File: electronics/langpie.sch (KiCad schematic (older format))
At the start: 0 parts

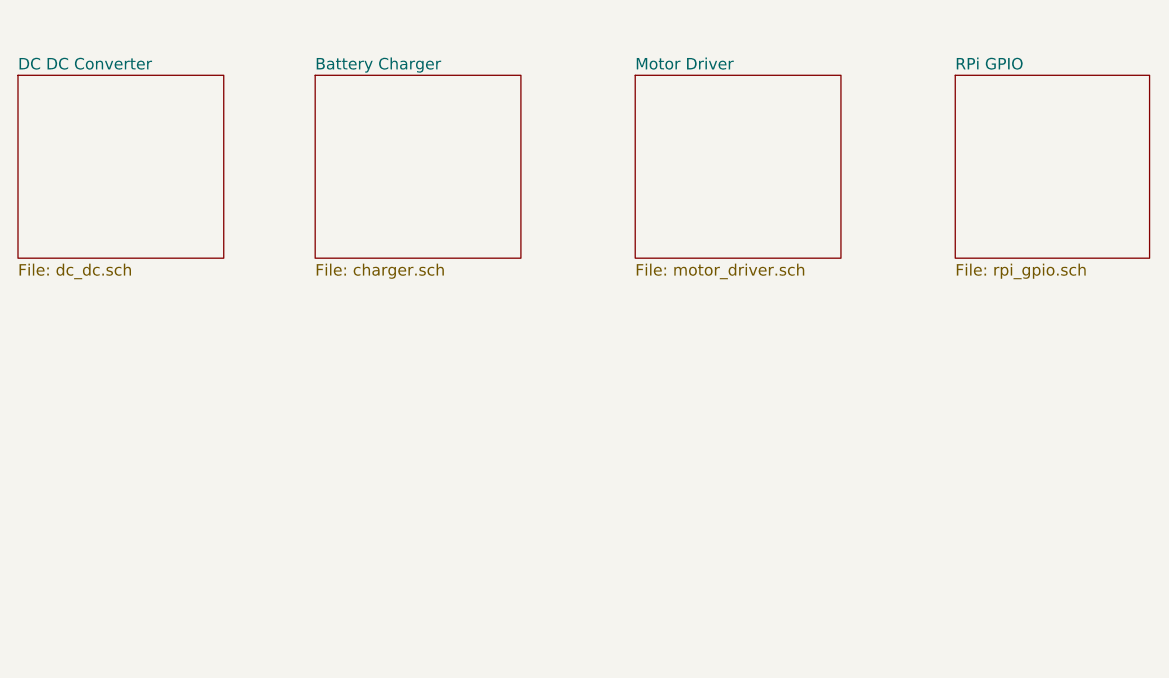
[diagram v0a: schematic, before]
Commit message: Change to electronics, and adding pi dimensions into documents
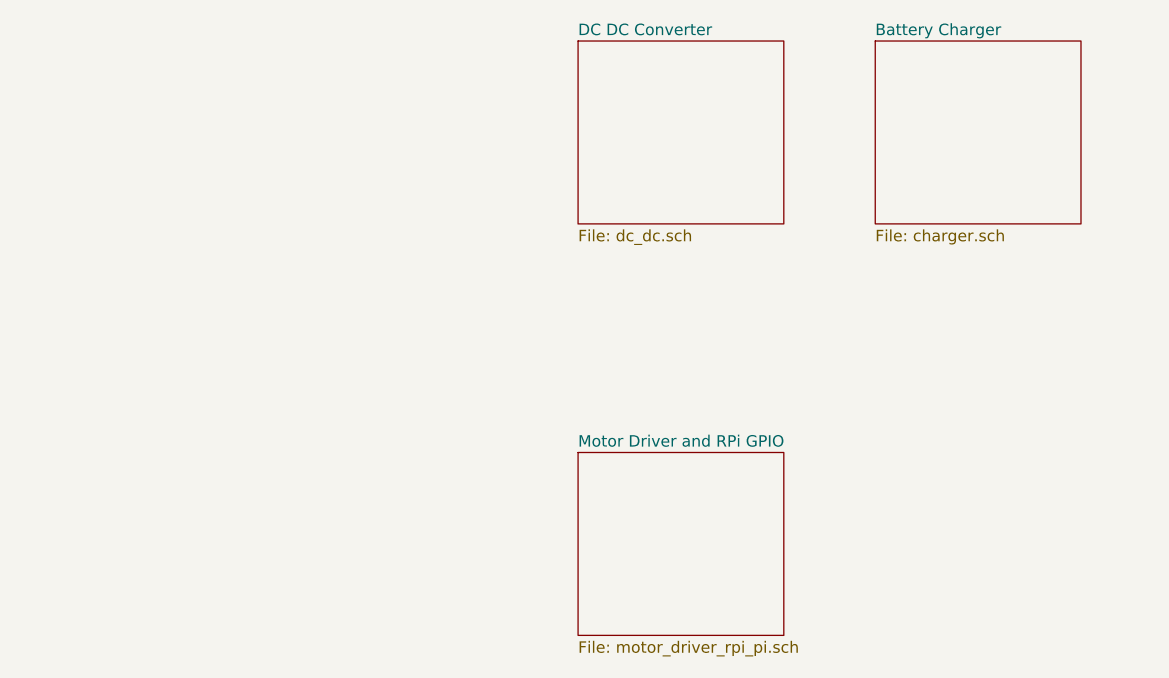
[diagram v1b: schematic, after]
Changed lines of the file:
@@
 $Descr A4 11693 8268
 encoding utf-8
-Sheet 1 5
+Sheet 1 4
 Title ""
 Date ""
@@
 $EndDescr
 $Sheet
-S 2350 2200 900  800
+S 4800 2050 900  800
 U 5E90B2B2
 F0 "DC DC Converter" 50
@@
 $EndSheet
 $Sheet
-S 3650 2200 900  800
+S 6100 2050 900  800
 U 5E915994
 F0 "Battery Charger" 50
@@
 $EndSheet
 $Sheet
-S 5050 2200 900  800
+S 4800 3850 900  800
 U 5E914BA5
-F0 "Motor Driver" 50
-F1 "motor_driver.sch" 50
-$EndSheet
-$Sheet
-S 6450 2200 850  800
-U 5E9108BA
-F0 "RPi GPIO" 50
-F1 "rpi_gpio.sch" 50
+F0 "Motor Driver and RPi GPIO" 50
+F1 "motor_driver_rpi_pi.sch" 50
 $EndSheet
 $EndSCHEMATC

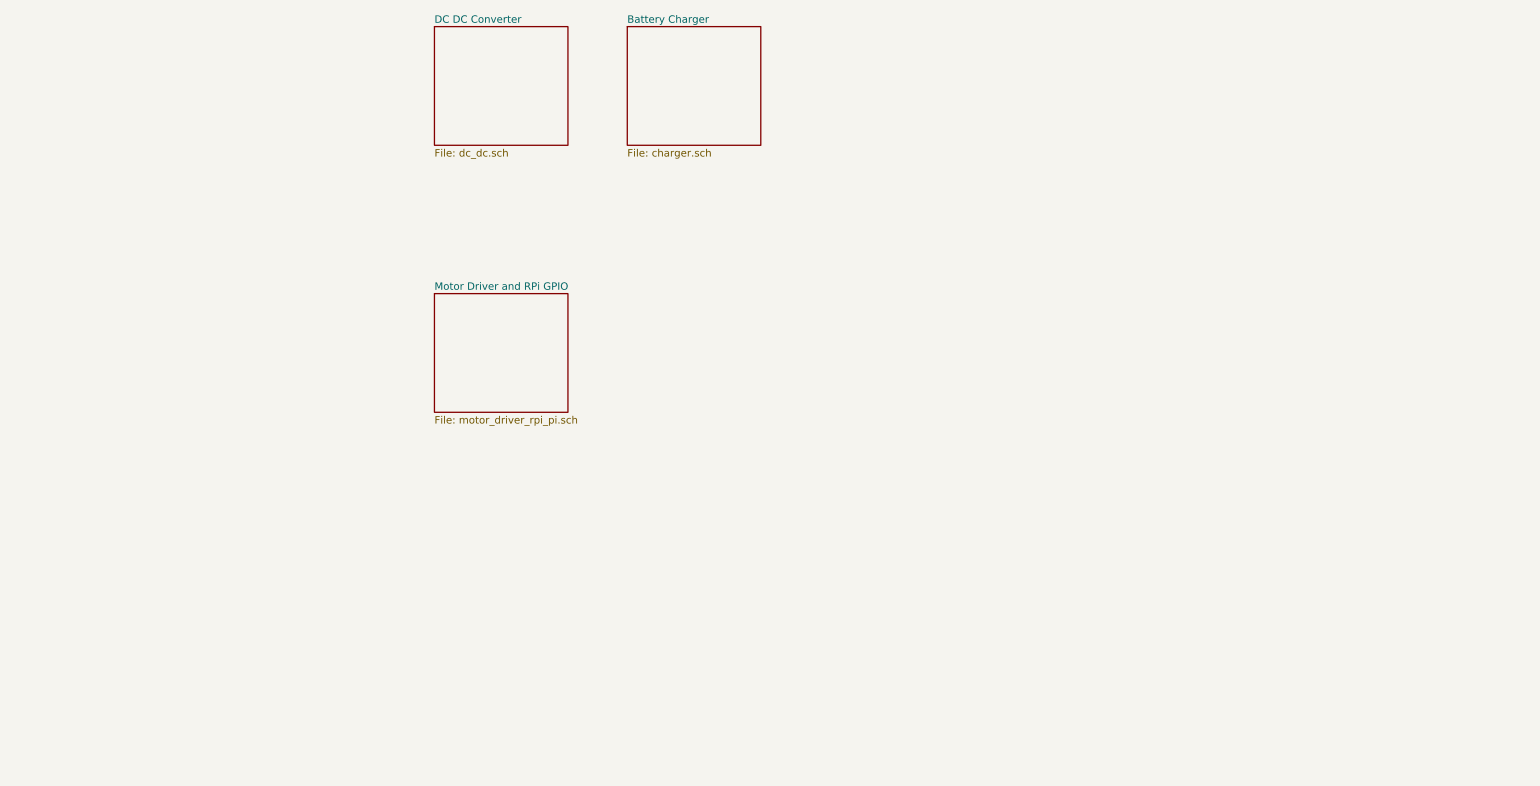
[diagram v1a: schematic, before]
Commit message: Preview SCH is done, but not fully finished.
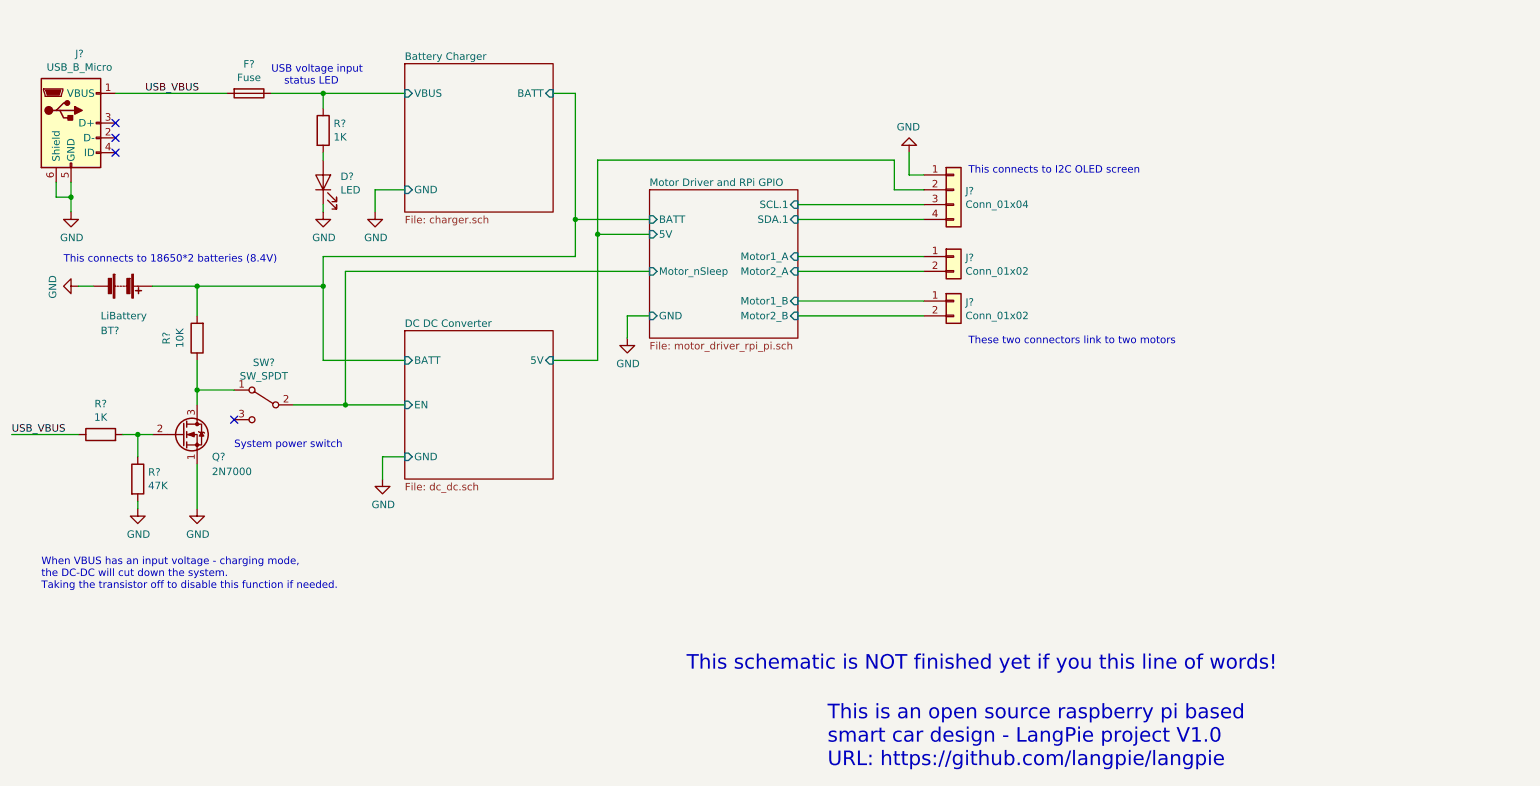
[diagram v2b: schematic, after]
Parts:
- added BT?: LiBattery, symbol Device:Battery
- added D?: LED, LED_SMD:LED_0805_2012Metric, symbol Device:LED
- added F?: Fuse, Fuse:Fuse_1206_3216Metric, symbol Device:Fuse
- added J?: USB_B_Micro, Connector_USB:USB_Micro-B_GCT_USB3076-30-A, symbol Connector:USB_B_Micro
- added J? (x2): Conn_01x02, Connector_Wire:SolderWirePad_1x02_P5.08mm_Drill1.5mm, symbol Connector_Generic:Conn_01x02
- added J?: Conn_01x04, Connector_PinHeader_2.54mm:PinHeader_1x04_P2.54mm_Vertical, symbol Connector_Generic:Conn_01x04
- added Q?: 2N7000, Package_TO_SOT_SMD:SOT-23, symbol Transistor_FET:2N7000
- added R? (x2): 1K, Resistor_SMD:R_0805_2012Metric, symbol Device:R
- added R?: 47K, Resistor_SMD:R_0805_2012Metric, symbol Device:R
- added R?: 10K, Resistor_SMD:R_0805_2012Metric, symbol Device:R
- added SW?: SW_SPDT, symbol Switch:SW_SPDT
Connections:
- new net: Q?.2 (G), R?.1, R?.2
- new net: Q?.3 (D), R?.1, SW?.1 (A)
- new net: D?.2 (A), R?.2
- new net Battery Charger/BATT: BT?.1 (+), R?.2
- new net Battery Charger/VBUS: F?.1, R?.1
- new net DC DC Converter/5V: J?.2 (Pin_2)
- new net DC DC Converter/EN: SW?.2 (B)
- new net GND: BT?.2 (-), D?.1 (K), J?.1 (Pin_1), J?.5 (GND), J?.6 (Shield), Q?.1 (S), R?.2
- new net Motor Driver and RPi GPIO/Motor1_A: J?.1 (Pin_1)
- new net Motor Driver and RPi GPIO/Motor1_B: J?.1 (Pin_1)
- new net Motor Driver and RPi GPIO/Motor2_A: J?.2 (Pin_2)
- new net Motor Driver and RPi GPIO/Motor2_B: J?.2 (Pin_2)
- new net Motor Driver and RPi GPIO/SCL.1: J?.3 (Pin_3)
- new net Motor Driver and RPi GPIO/SDA.1: J?.4 (Pin_4)
- new net USB_VBUS: F?.2, J?.1 (VBUS), R?.1
- no-connect marks 0 -> 4
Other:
- note added: "System power switch"
- note added: "These two connectors link to two motors\n"
- note added: "This connects to 18650*2 batteries (8.4V)"
- note added: "This connects to I2C OLED screen\n"
- note added: "This is an open source raspberry pi based \nsmart car design - LangPie project V1.0\nURL: https://github.com/langpie/langpie"
- note added: "This schematic is NOT finished yet if you this line of words!\n"
- note added: "USB voltage input \n status LED"
- note added: "When VBUS has an input voltage - charging mode, \nthe DC-DC will cut down the system. \nTaking the transistor off to disable this function if needed.\n"
